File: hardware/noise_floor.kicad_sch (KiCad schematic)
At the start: 33 parts, among them J1 DC Power, J10 IO/Switch Connector 1 (Switch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, J11 IO/Switch Connector 2 (Switch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, J2 Input, J3 Output, J4 UX1, J5 UX2, J6 Battery, J7 IO/Effect Connector 1 (IO Sid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, J8 IO/Switch Connector 1 (IO Sid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, J9 IO/Switch Connector 2 (IO Sid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, SW1 Footswitch, SW2 SPDT1, SW3 SPDT2, SW4 SPDT3

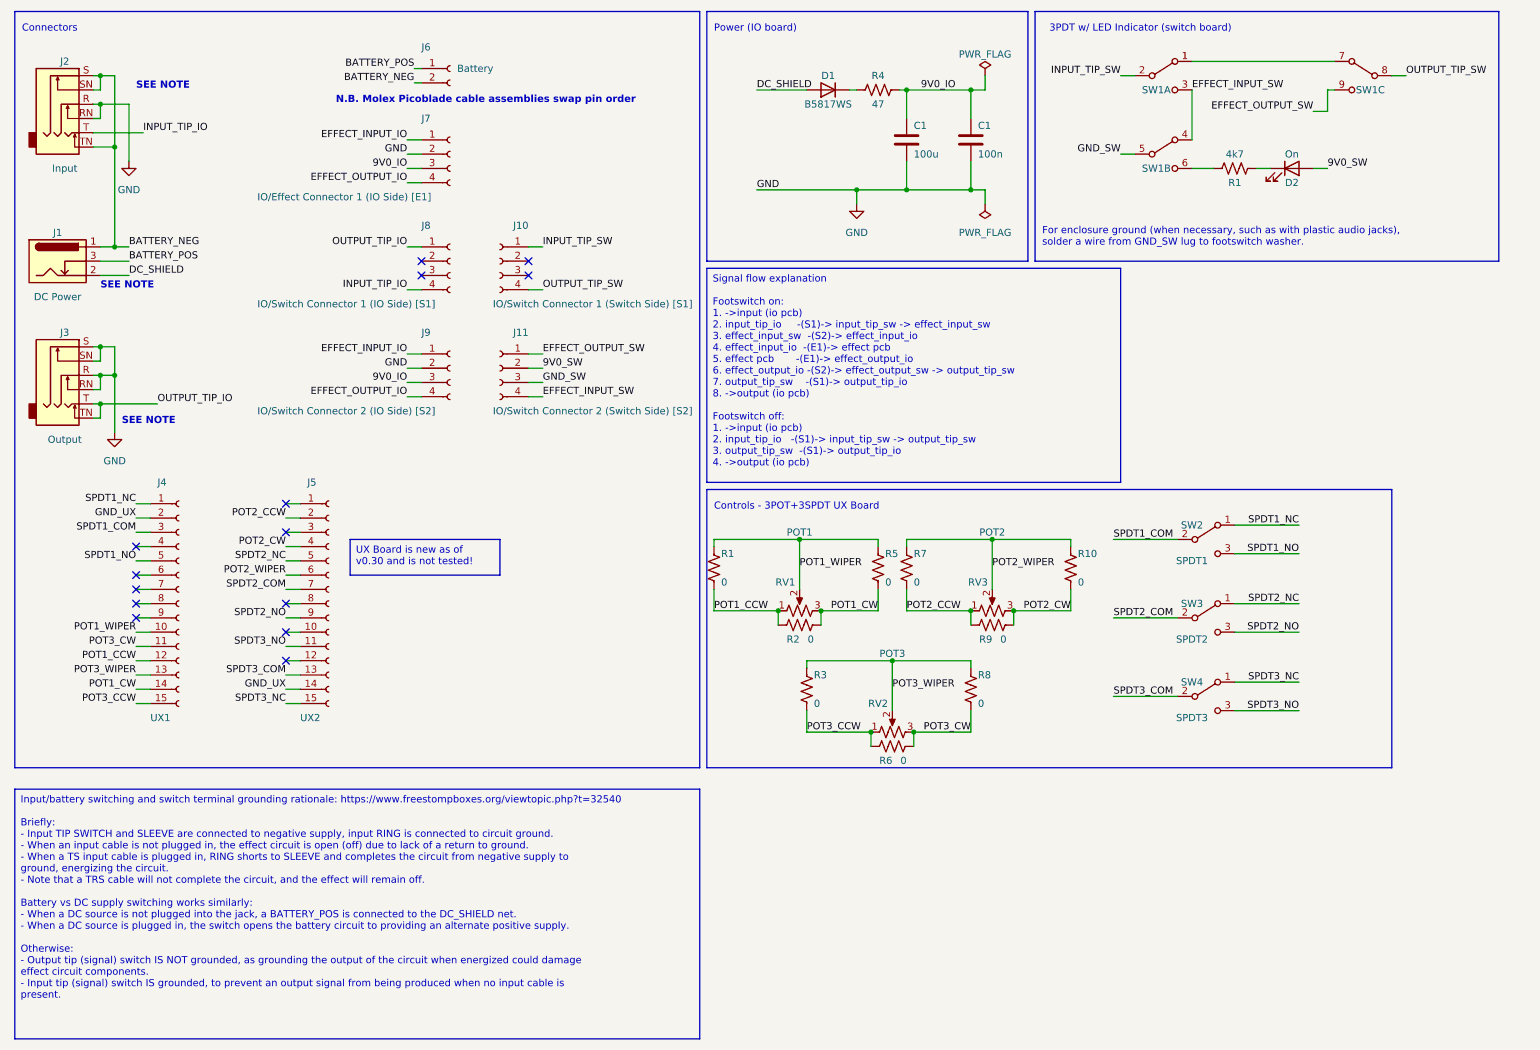
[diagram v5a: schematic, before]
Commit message: Further iteration on UX board:
 - Change to square body pots and bump count to six
 - Change to 25-pin board-to-board connectors (and improve footprint)
 - Change optional pot adjustment to 1206 smt resistors
 - Update layout/routing to suit
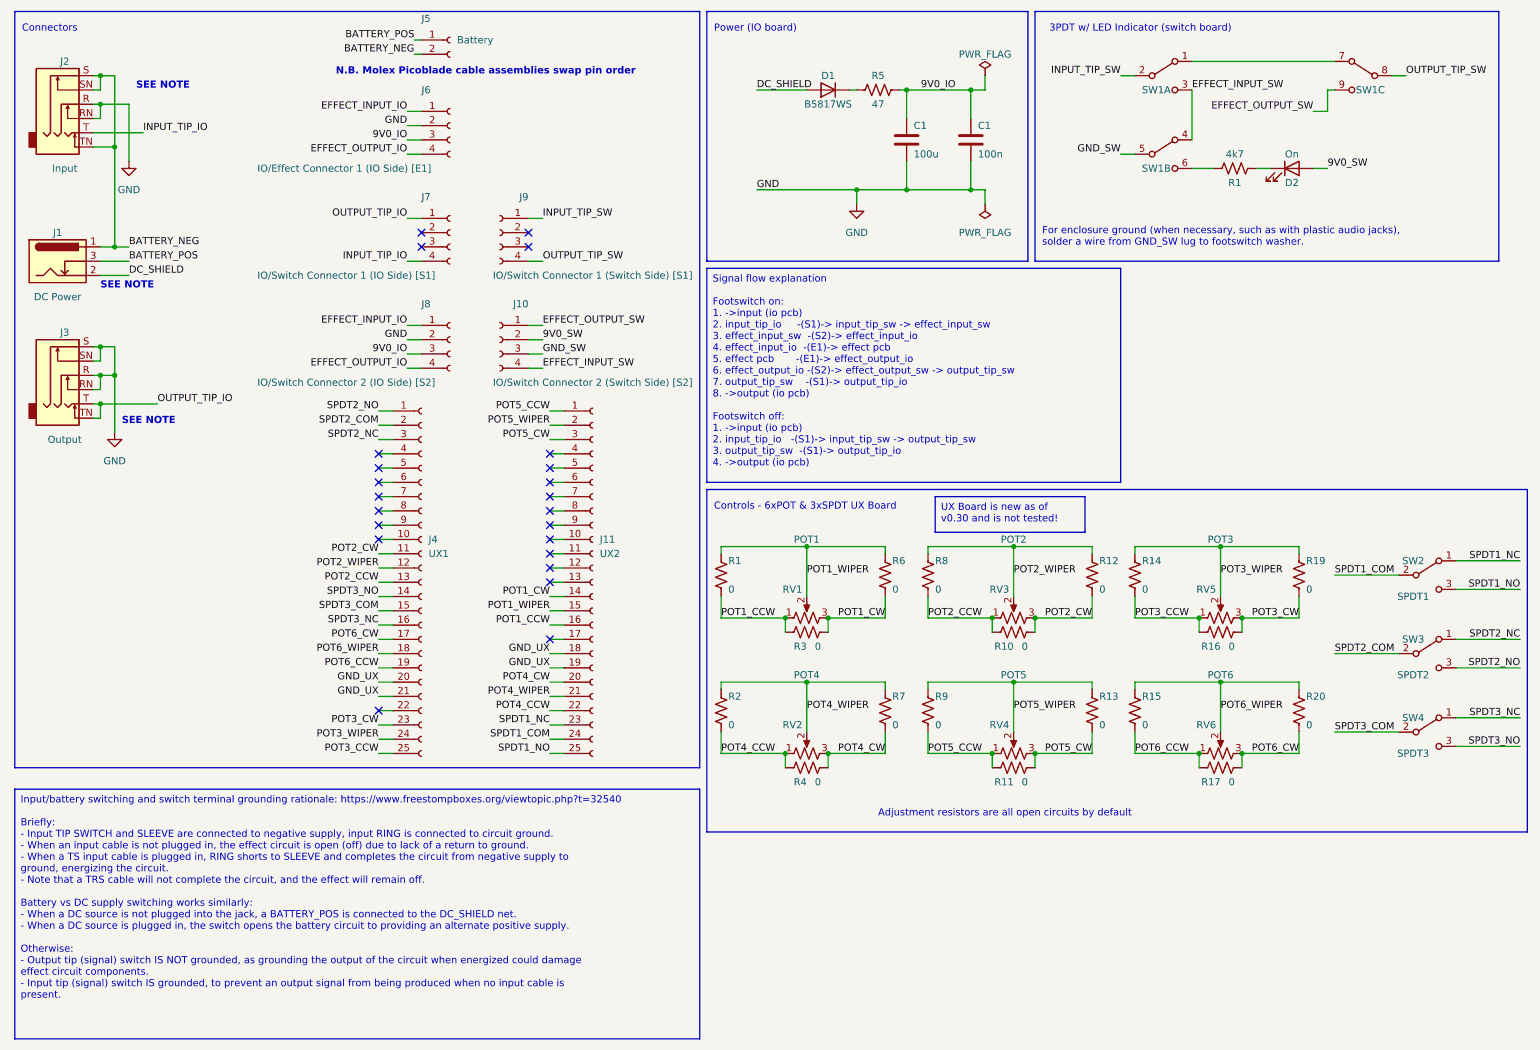
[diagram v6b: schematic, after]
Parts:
- added R11, R13, R15, R17, R2, R20, R4, R7, R9: 0, Resistor_SMD:R_1206_3216Metric_Pad1.30x1.75mm_HandSolder, symbol Device:R_US
- added RV2: POT4, noise_floor:Potentiometer_Alpha_RD901F-40-00D_Single_Vertical_with_3DModel_from_Vasily_Kashirin, symbol Device:R_Potentiometer_US
- added RV4: POT5, noise_floor:Potentiometer_Alpha_RD901F-40-00D_Single_Vertical_with_3DModel_from_Vasily_Kashirin, symbol Device:R_Potentiometer_US
- added RV6: POT6, noise_floor:Potentiometer_Alpha_RD901F-40-00D_Single_Vertical_with_3DModel_from_Vasily_Kashirin, symbol Device:R_Potentiometer_US
- J11: renamed from J5; footprint noise_floor:Amphenol_Receptacle_15pin_10162581-3134115LF -> noise_floor:Amphenol_Receptacle_25pin_10162581-3134125LF; symbol Connector:Conn_01x15_Socket -> Connector:Conn_01x25_Socket
- J4: footprint noise_floor:Amphenol_Receptacle_15pin_10162581-3134115LF -> noise_floor:Amphenol_Receptacle_25pin_10162581-3134125LF; symbol Connector:Conn_01x15_Socket -> Connector:Conn_01x25_Socket
- R1: footprint Resistor_THT:R_Axial_DIN0207_L6.3mm_D2.5mm_P7.62mm_Horizontal -> Resistor_SMD:R_1206_3216Metric_Pad1.30x1.75mm_HandSolder
- R10: renamed from R9; footprint Resistor_THT:R_Axial_DIN0207_L6.3mm_D2.5mm_P7.62mm_Horizontal -> Resistor_SMD:R_1206_3216Metric_Pad1.30x1.75mm_HandSolder
- R12: renamed from R10; footprint Resistor_THT:R_Axial_DIN0207_L6.3mm_D2.5mm_P7.62mm_Horizontal -> Resistor_SMD:R_1206_3216Metric_Pad1.30x1.75mm_HandSolder
- R14: renamed from R3; footprint Resistor_THT:R_Axial_DIN0207_L6.3mm_D2.5mm_P7.62mm_Horizontal -> Resistor_SMD:R_1206_3216Metric_Pad1.30x1.75mm_HandSolder
- R16: renamed from R6; footprint Resistor_THT:R_Axial_DIN0207_L6.3mm_D2.5mm_P7.62mm_Horizontal -> Resistor_SMD:R_1206_3216Metric_Pad1.30x1.75mm_HandSolder
- R19: renamed from R8; footprint Resistor_THT:R_Axial_DIN0207_L6.3mm_D2.5mm_P7.62mm_Horizontal -> Resistor_SMD:R_1206_3216Metric_Pad1.30x1.75mm_HandSolder
- R3: renamed from R2; footprint Resistor_THT:R_Axial_DIN0207_L6.3mm_D2.5mm_P7.62mm_Horizontal -> Resistor_SMD:R_1206_3216Metric_Pad1.30x1.75mm_HandSolder
- R6: renamed from R5; footprint Resistor_THT:R_Axial_DIN0207_L6.3mm_D2.5mm_P7.62mm_Horizontal -> Resistor_SMD:R_1206_3216Metric_Pad1.30x1.75mm_HandSolder
- R8: renamed from R7; footprint Resistor_THT:R_Axial_DIN0207_L6.3mm_D2.5mm_P7.62mm_Horizontal -> Resistor_SMD:R_1206_3216Metric_Pad1.30x1.75mm_HandSolder
- RV1, RV3: footprint noise_floor:Potentiometer_Single_3_Horizontal -> noise_floor:Potentiometer_Alpha_RD901F-40-00D_Single_Vertical_with_3DModel_from_Vasily_Kashirin
- RV5: renamed from RV2; footprint noise_floor:Potentiometer_Single_3_Horizontal -> noise_floor:Potentiometer_Alpha_RD901F-40-00D_Single_Vertical_with_3DModel_from_Vasily_Kashirin
- renumbered J11 to J10, J6 to J5, J7 to J6, J8 to J7, J9 to J8, J10 to J9, R4 to R5
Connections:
- net GND_UX: now also J11.18 (Pin_18), J11.19 (Pin_19), J4.20 (Pin_20), J4.21 (Pin_21); no longer J11.14 (Pin_14), J4.2 (Pin_2)
- net POT1_CCW: now also J11.16 (Pin_16); no longer J4.12 (Pin_12)
- net POT1_CW: now also J11.14 (Pin_14); no longer J4.14 (Pin_14)
- net POT1_WIPER: now also J11.15 (Pin_15); no longer J4.10 (Pin_10)
- net POT2_CCW: now also J4.13 (Pin_13); no longer J11.2 (Pin_2)
- net POT2_CW: now also J4.11 (Pin_11); no longer J11.4 (Pin_4)
- net POT2_WIPER: now also J4.12 (Pin_12); no longer J11.6 (Pin_6)
- net POT3_CCW: now also J4.25 (Pin_25); no longer J4.15 (Pin_15)
- net POT3_CW: now also J4.23 (Pin_23); no longer J4.11 (Pin_11)
- net POT3_WIPER: now also J4.24 (Pin_24); no longer J4.13 (Pin_13)
- net SPDT1_COM: now also J11.24 (Pin_24); no longer J4.3 (Pin_3)
- net SPDT1_NC: now also J11.23 (Pin_23); no longer J4.1 (Pin_1)
- net SPDT1_NO: now also J11.25 (Pin_25); no longer J4.5 (Pin_5)
- net SPDT2_COM: now also J4.2 (Pin_2); no longer J11.7 (Pin_7)
- net SPDT2_NC: now also J4.3 (Pin_3); no longer J11.5 (Pin_5)
- net SPDT2_NO: now also J4.1 (Pin_1); no longer J11.9 (Pin_9)
- net SPDT3_COM: now also J4.15 (Pin_15); no longer J11.13 (Pin_13)
- net SPDT3_NC: now also J4.16 (Pin_16); no longer J11.15 (Pin_15)
- net SPDT3_NO: now also J4.14 (Pin_14); no longer J11.11 (Pin_11)
- net POT5_CCW: now reaches J11.1 (Pin_1)
- net POT5_CCW: now also R11.2, R9.1, RV4.1
- net POT5_CW: now reaches J11.3 (Pin_3)
- net POT5_CW: now also R11.1, R13.1, RV4.3
- new net POT4_CCW: J11.22 (Pin_22), R2.1, R4.2, RV2.1
- new net POT4_CW: J11.20 (Pin_20), R4.1, R7.1, RV2.3
- new net POT4_WIPER: J11.21 (Pin_21), R2.2, R7.2, RV2.2
- new net POT5_WIPER: J11.2 (Pin_2), R13.2, R9.2, RV4.2
- new net POT6_CCW: J4.19 (Pin_19), R15.1, R17.2, RV6.1
- new net POT6_CW: J4.17 (Pin_17), R17.1, R20.1, RV6.3
- new net POT6_WIPER: J4.18 (Pin_18), R15.2, R20.2, RV6.2
- no-connect marks 14 -> 23
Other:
- note added: "Adjustment resistors are all open circuits by default"
- note added: "Controls - 6xPOT & 3xSPDT UX Board"
- note removed: "Controls - 3POT+3SPDT UX Board"
- moved on the sheet: J10, J5, J6, J7, J8, J9, R1, R10, R12, R14, R16, R19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

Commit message: minor tweaks to schematic layout
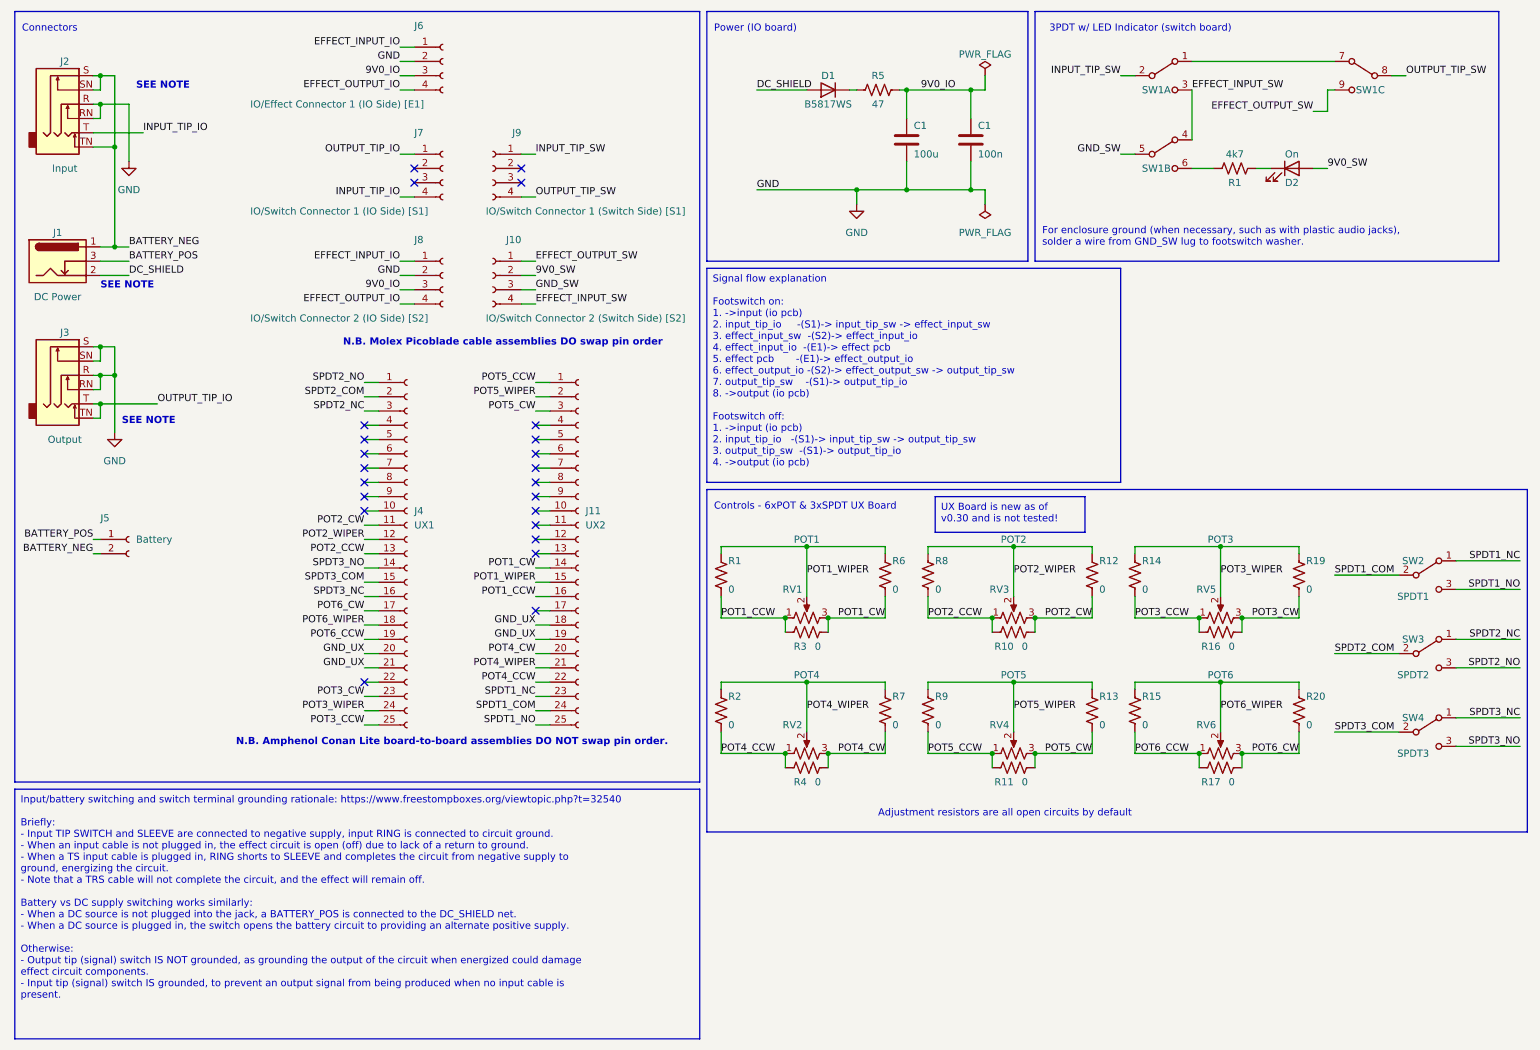
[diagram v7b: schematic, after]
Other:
- note added: "N.B. Amphenol Conan Lite board-to-board assemblies DO NOT swap pin order."
- note added: "N.B. Molex Picoblade cable assemblies DO swap pin order"
- note removed: "N.B. Molex Picoblade cable assemblies swap pin order"
- moved on the sheet: J10, J11, J4, J5, J6, J7, J8, J9
